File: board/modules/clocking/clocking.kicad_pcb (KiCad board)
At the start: 2 copper layers, 38 parts, among them SW1 CLK, SW2 SEL, U1 NE555D, U2 NE555D, U3 NE555D, U4 NE555D, U5 7404, U6 7400, U7 7400, U8 7400

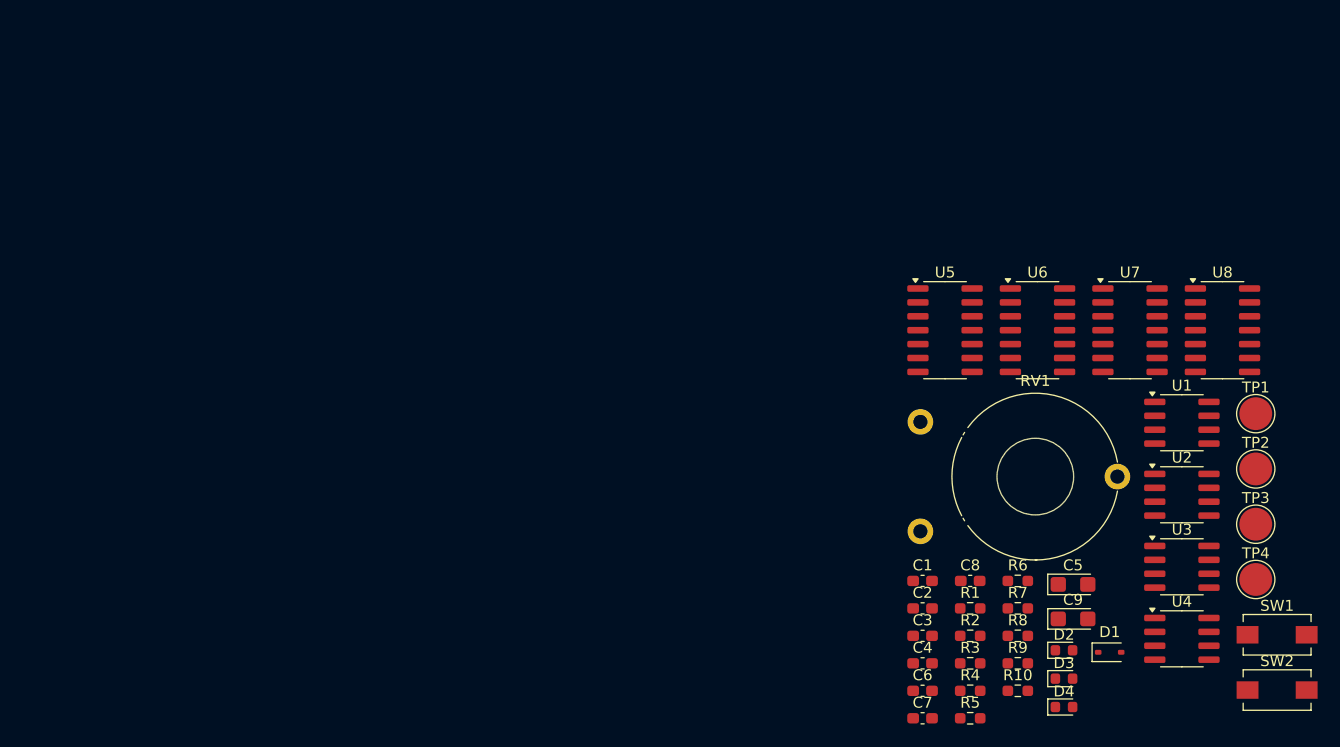
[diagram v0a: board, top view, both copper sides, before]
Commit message: Correction in Astable
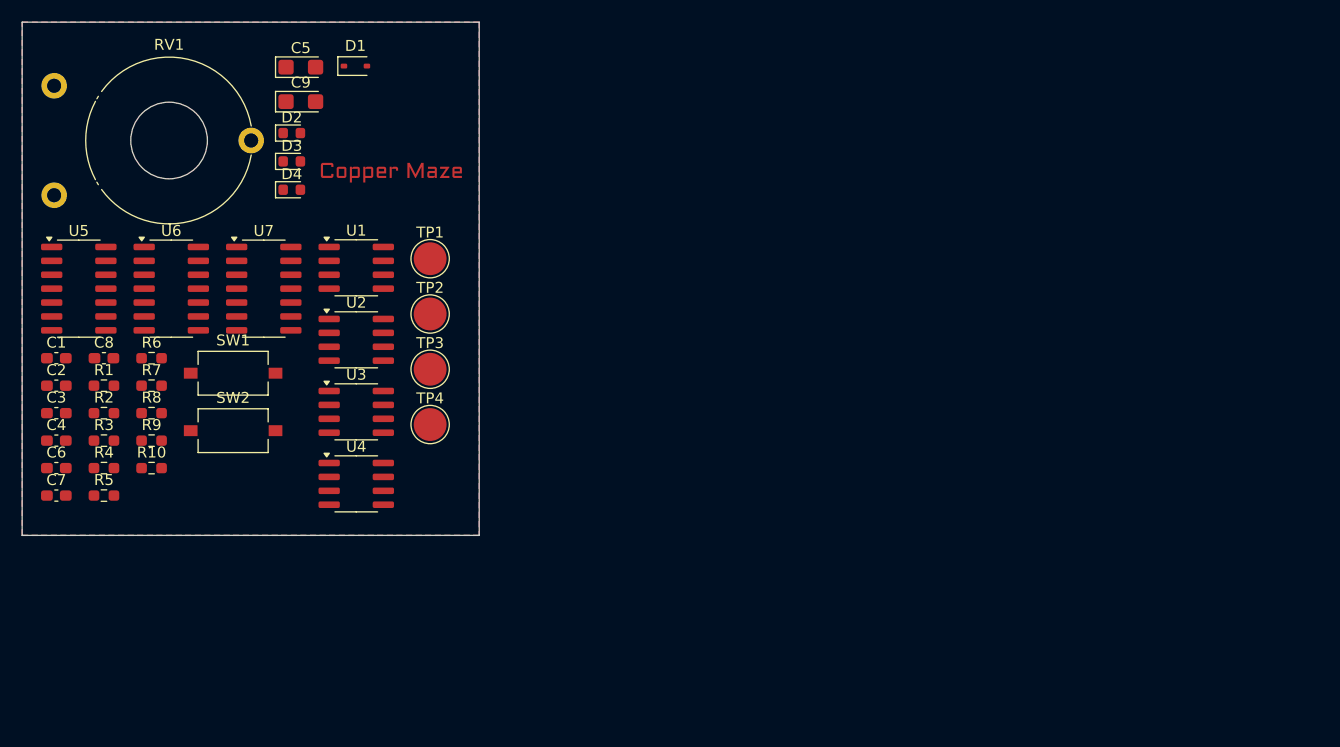
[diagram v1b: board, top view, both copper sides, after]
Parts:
- removed U8: 7400, 8bitcomp:SOIC-14_3.9x8.7mm_P1.27mm
- SW1, SW2: footprint 8bitcomp:SW_SPST_EVQPE1 -> 8bitcomp:SW_Tactile_SPST_NO_Straight_CK_PTS636Sx25SMTRLFS
- U1, U2, U3, U4: footprint 8bitcomp:SOIC-8_3.9x4.9mm_P1.27mm -> Package_SO:SOIC-8_3.9x4.9mm_P1.27mm
- moved SW1 98.3 mm to (46.7, 57.4)
- moved SW2 98.3 mm to (46.7, 62.6)
- moved D1 87.3 mm to (57.8, 29.3)
- moved C9 84.9 mm to (52.8, 32.6)
- moved D2 84.9 mm to (52.0, 35.5)
- moved D3 84.9 mm to (52.0, 38.0)
- moved D4 84.9 mm to (52.0, 40.6)
- moved C5 84.9 mm to (52.8, 29.4)
- moved RV1 84.9 mm to (30.3, 41.1)
- moved C8 81.7 mm to (34.9, 56.0)
- moved R1 81.7 mm to (34.9, 58.5)
- moved R3 81.7 mm to (34.9, 63.6)
- moved R4 81.7 mm to (34.9, 66.1)
- moved C1 81.7 mm to (30.5, 56.0)
- moved C2 81.7 mm to (30.5, 58.5)
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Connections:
- U5 pad 12: (no net) -> unconnected-(U5-Pad12)
- U5 pad 13: (no net) -> unconnected-(U5-Pad13)
- U6 pad 1: (no net) -> /FRC
- U6 pad 2: (no net) -> Net-(D2-A)
- U6 pad 3: (no net) -> /FRC_rst_sync
- U7 pad 10: Net-(U7-Pad10) -> /MCC_rst_sync
- U7 pad 6: Net-(U7-Pad10) -> /MCC_rst_sync
- U7 pad 9: Net-(U7-Pad9) -> /FRC_rst_sync
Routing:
- added copper zone on B.Cu, net GND
- added copper zone on F.Cu, net GND
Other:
- board outline added: 41.8 x 46.9 mm
